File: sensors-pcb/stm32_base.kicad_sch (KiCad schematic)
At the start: 41 parts

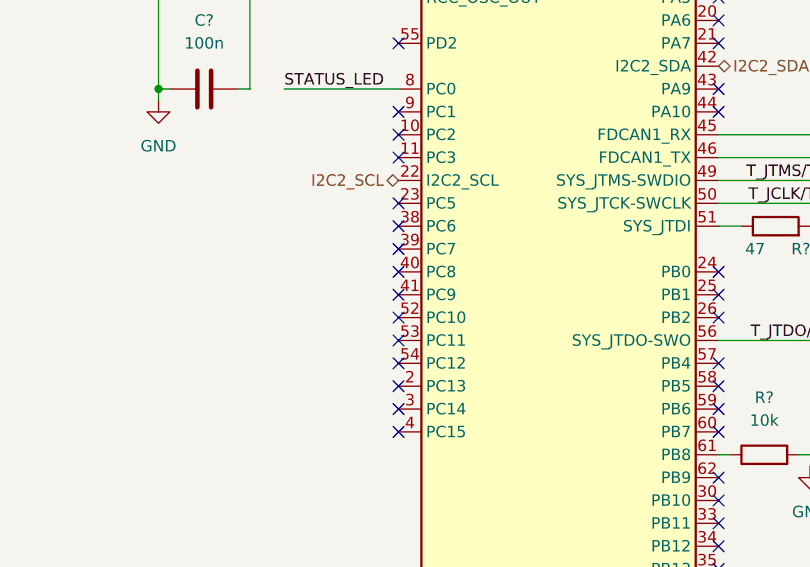
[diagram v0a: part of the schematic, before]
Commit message: sensors-pcb: finish GPS schematic
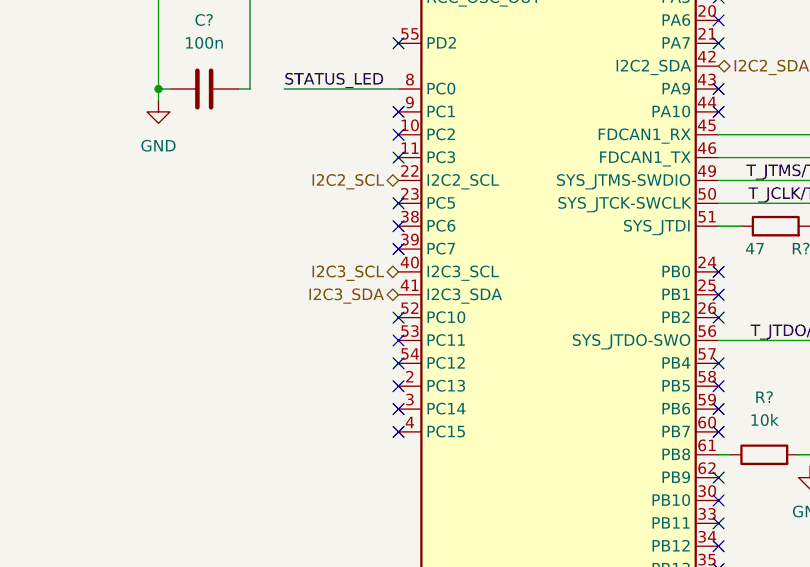
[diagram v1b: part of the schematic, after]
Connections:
- net I2C3_SCL: now reaches U?.40 (PC8)
- net I2C3_SDA: now reaches U?.41 (PC9)
- no-connect marks 40 -> 38
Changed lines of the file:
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@@
-	)
-	(no_connect
-		(at 63.5 138.43)
 	)
 	(no_connect
 		(at 63.5 113.03)
-	)
-	(no_connect
-		(at 63.5 140.97)
 	)
 	(no_connect
@@
 			)
 			(justify left)
+		)
+	)
+	(hierarchical_label "I2C3_SCL"
+		(shape bidirectional)
+		(at 63.5 138.43 180)
+		(effects
+			(font
+				(size 1.27 1.27)
+			)
+			(justify right)
+		)
+	)
+	(hierarchical_label "I2C3_SDA"
+		(shape bidirectional)
+		(at 63.5 140.97 180)
+		(effects
+			(font
+				(size 1.27 1.27)
+			)
+			(justify right)
 		)
 	)
@@
 		)
 		(pin "40"
+			(alternate "I2C3_SCL")
 		)
 		(pin "62"
@@
 		)
 		(pin "41"
+			(alternate "I2C3_SDA")
 		)
 		(pin "42"

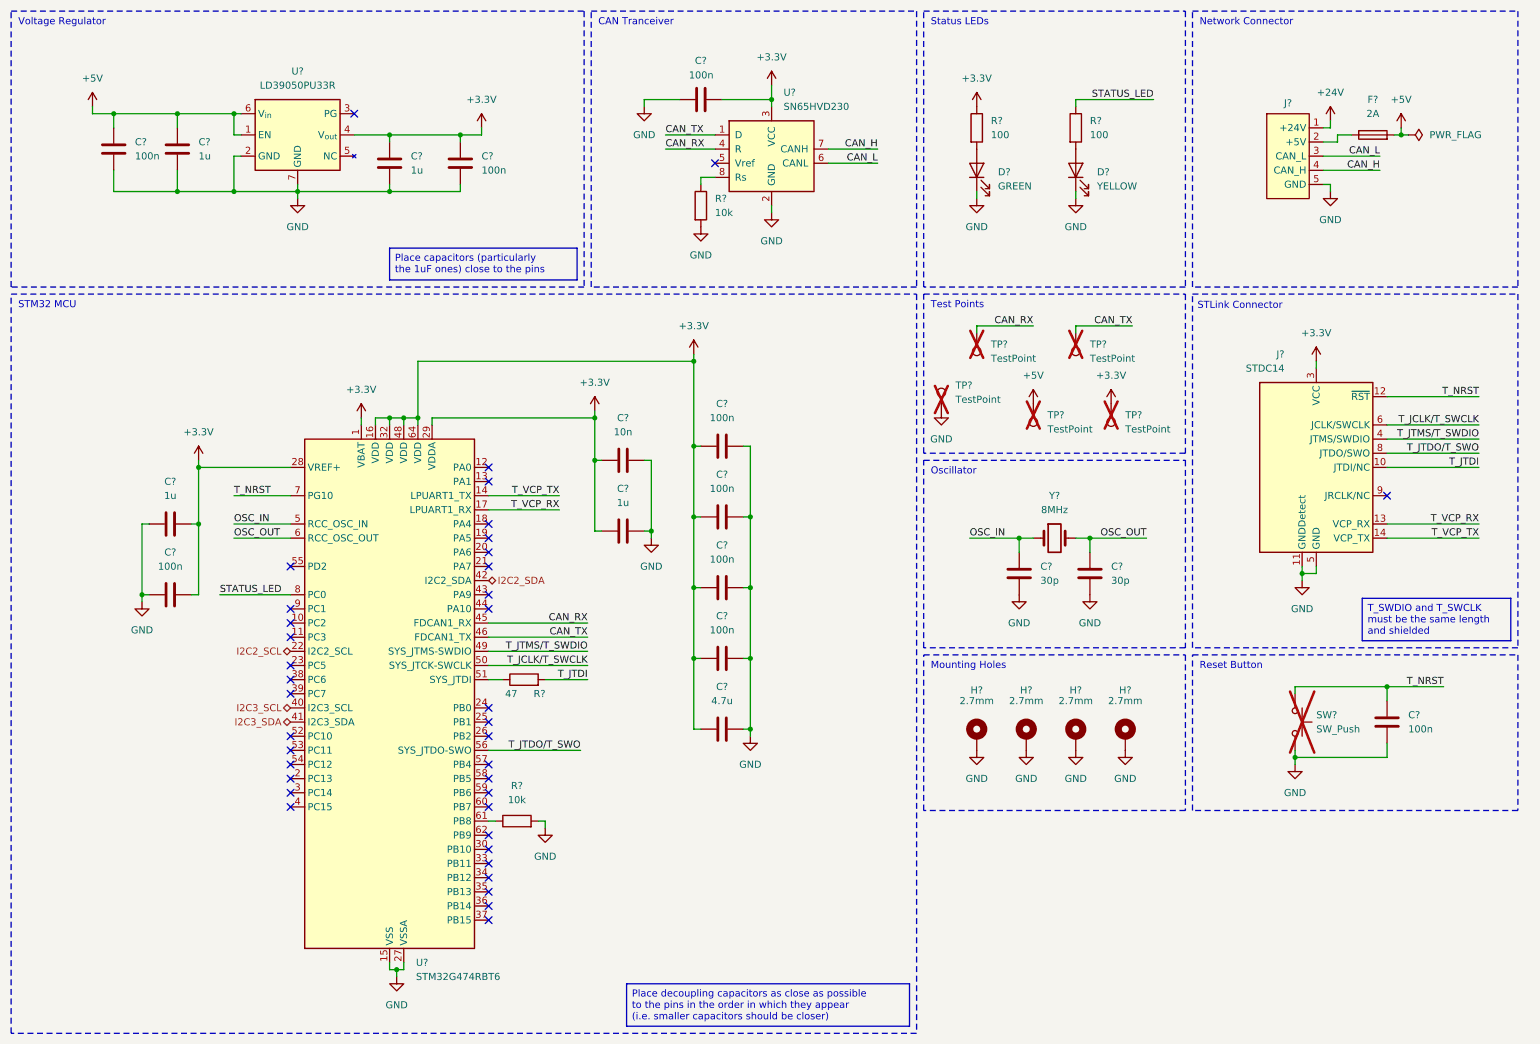
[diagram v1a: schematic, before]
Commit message: sensors-pcb: add footprints
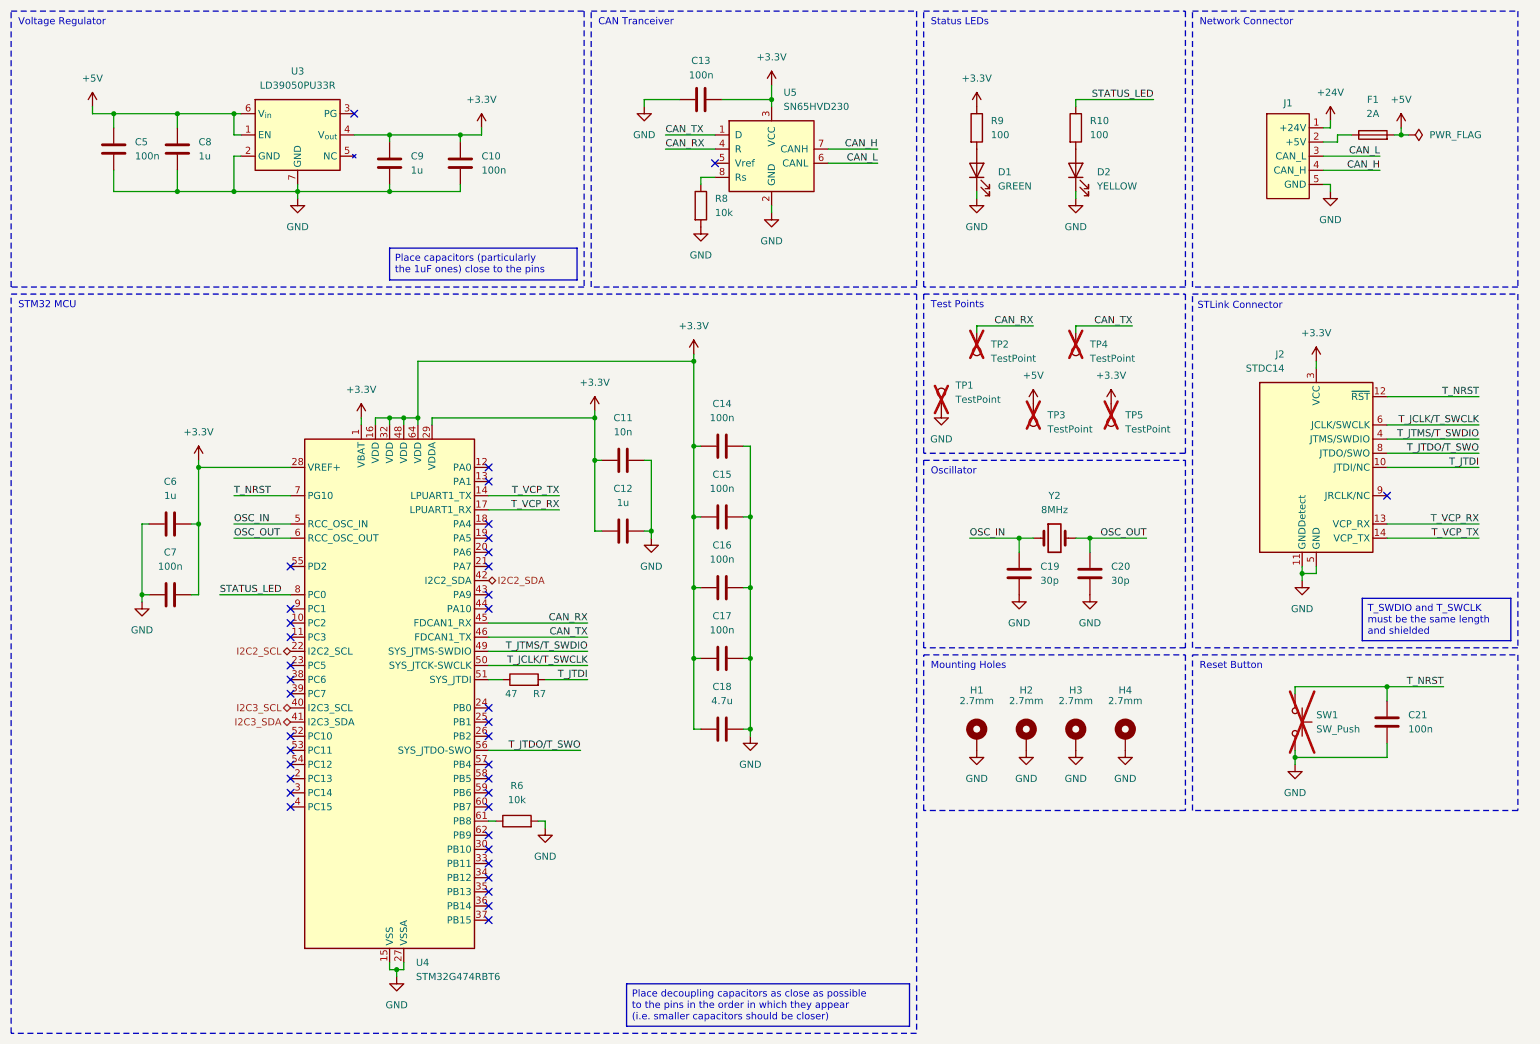
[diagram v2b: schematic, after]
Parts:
- gave numbers to parts that had none: 41

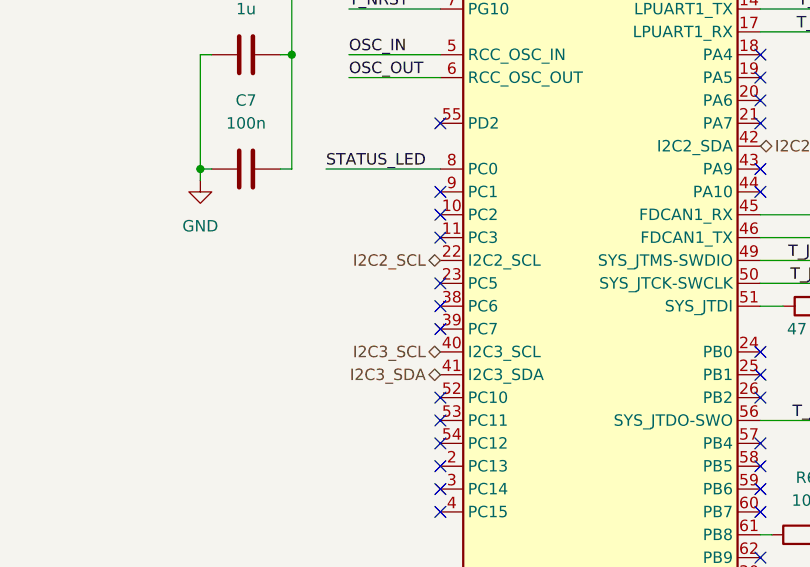
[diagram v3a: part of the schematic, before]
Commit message: sensors-pcb: replace IMU with MPU-6050
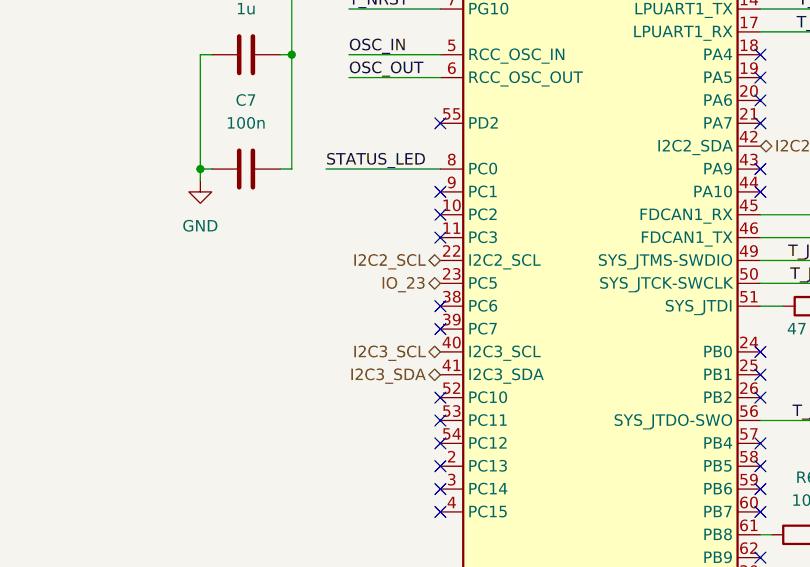
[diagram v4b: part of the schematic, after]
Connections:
- net IO_23: now reaches U4.23 (PC5)
- no-connect marks 38 -> 37
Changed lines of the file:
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@@
-	)
-	(no_connect
-		(at 63.5 130.81)
 	)
 	(no_connect
@@
 		)
 	)
+	(hierarchical_label "IO_23"
+		(shape bidirectional)
+		(at 63.5 130.81 180)
+		(effects
+			(font
+				(size 1.27 1.27)
+			)
+			(justify right)
+		)
+	)

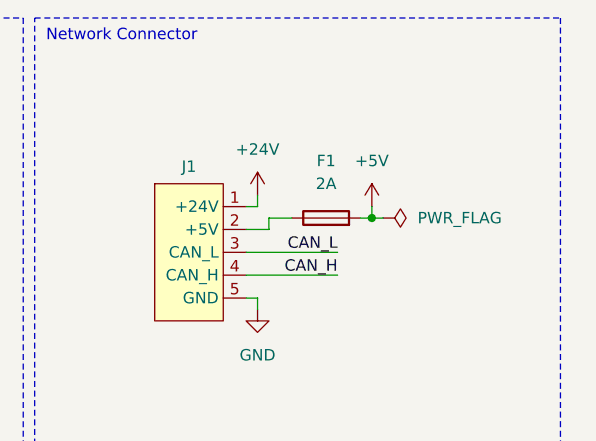
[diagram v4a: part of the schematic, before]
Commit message: sensors-pcb: add test point for fuse
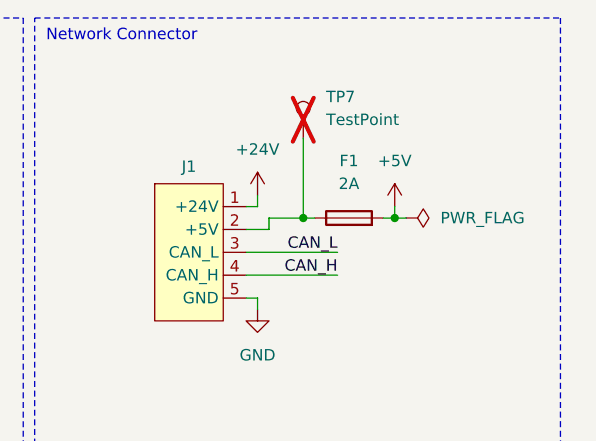
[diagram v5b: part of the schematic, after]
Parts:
- added TP4: TestPoint, TestPoint:TestPoint_Keystone_5005-5009_Compact, symbol Connector:TestPoint
- renumbered TP4 to TP7
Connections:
- net CAN_TX: now also TP4.1; no longer TP7.1
- net at F1.1, J1.2 (+5V): now also TP7.1
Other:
- moved on the sheet: F1, TP7
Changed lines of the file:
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@@
 	)
 	(junction
-		(at 262.89 35.56)
+		(at 265.43 35.56)
+		(diameter 0)
+		(color 0 0 0 0)
+	)
+	(junction
+		(at 255.27 35.56)
 		(diameter 0)
 		(color 0 0 0 0)
@@
 	(wire
 		(pts
-			(xy 251.46 35.56) (xy 254 35.56)
+			(xy 251.46 35.56) (xy 255.27 35.56)
 		)
 		(stroke
@@
 	(wire
 		(pts
-			(xy 262.89 34.29) (xy 262.89 35.56)
+			(xy 265.43 34.29) (xy 265.43 35.56)
 		)
 		(stroke
@@
 	(wire
 		(pts
-			(xy 261.62 35.56) (xy 262.89 35.56)
+			(xy 264.16 35.56) (xy 265.43 35.56)
 		)
 		(stroke
@@
 	(wire
 		(pts
-			(xy 262.89 35.56) (xy 264.16 35.56)
+			(xy 265.43 35.56) (xy 266.7 35.56)
 		)
 		(stroke
@@
 	(wire
 		(pts
+			(xy 256.54 35.56) (xy 255.27 35.56)
+		)
+		(stroke
+			(width 0)
+			(type default)
+		)
+	)
+	(wire
+		(pts
+			(xy 255.27 35.56) (xy 255.27 26.67)
+		)
+		(stroke
+			(width 0)
+			(type default)
+		)
+	)
+	(wire
+		(pts
 			(xy 146.05 104.14) (xy 146.05 116.84)
 		)
@@
 	(symbol
 		(lib_id "power:+5V")
-		(at 262.89 34.29 0)
+		(at 265.43 34.29 0)
 		(unit 1)
 		(exclude_from_sim no)
@@
 		(fields_autoplaced yes)
 		(property "Reference" "#PWR0132"
-			(at 262.89 38.1 0)
+			(at 265.43 38.1 0)
 			(effects
 				(font
@@
 		)
 		(property "Value" "+5V"
-			(at 262.89 29.21 0)
+			(at 265.43 29.21 0)
 			(effects
 				(font
@@
 		)
 		(property "Footprint" ""
-			(at 262.89 34.29 0)
+			(at 265.43 34.29 0)
 			(effects
 				(font
@@
 		)
 		(property "Datasheet" ""
-			(at 262.89 34.29 0)
+			(at 265.43 34.29 0)
 			(effects
 				(font
@@
 		)
 		(property "Description" "Power symbol creates a global label with name \"+5V\""
-			(at 262.89 34.29 0)
+			(at 265.43 34.29 0)
 			(effects
 				(font
@@
 	(symbol
 		(lib_id "Device:Fuse")
-		(at 257.81 35.56 90)
+		(at 260.35 35.56 90)
 		(unit 1)
 		(exclude_from_sim no)
@@
 		(fields_autoplaced yes)
 		(property "Reference" "F1"
-			(at 257.81 29.21 90)
+			(at 260.35 29.21 90)
 			(effects
 				(font
@@
 		)
 		(property "Value" "2A"
-			(at 257.81 31.75 90)
+			(at 260.35 31.75 90)
 			(effects
 				(font
@@
 		)
 		(property "Footprint" "Exocet:Fuse_Holder_Littelfuse_01530008"
-			(at 257.81 37.338 90)
+			(at 260.35 37.338 90)
 			(effects
 				(font
@@
 		)
 		(property "Datasheet" "~"
-			(at 257.81 35.56 0)
+			(at 260.35 35.56 0)
 			(effects
 				(font
@@
 		)
 		(property "Description" "Fuse"
-			(at 257.81 35.56 0)
+			(at 260.35 35.56 0)
 			(effects
 				(font
@@
 		)
 		(property "JLCPCB" "C206907"
-			(at 257.81 35.56 0)
+			(at 260.35 35.56 0)
 			(effects
 				(font
@@
 	(symbol
 		(lib_id "Connector:TestPoint")
+		(at 255.27 26.67 0)
+		(unit 1)
+		(exclude_from_sim no)
+		(in_bom yes)
+		(on_board yes)
+		(dnp yes)
+		(fields_autoplaced yes)
+		(property "Reference" "TP7"
+			(at 257.81 22.0979 0)
+			(effects
+				(font
+					(size 1.27 1.27)
+				)
+				(justify left)
+			)
+		)
+		(property "Value" "TestPoint"
+			(at 257.81 24.6379 0)
+			(effects
+				(font
+					(size 1.27 1.27)
+				)
+				(justify left)
+			)
+		)
+		(property "Footprint" "TestPoint:TestPoint_Keystone_5005-5009_Compact"
+			(at 260.35 26.67 0)
+			(effects
+				(font
+					(size 1.27 1.27)
+				)
+				(hide yes)
+			)
+		)
+		(property "Datasheet" "https://www.keyelco.com/userAssets/file/M65p56.pdf"
+			(at 260.35 26.67 0)
+			(effects
+				(font
+					(size 1.27 1.27)
+				)
+				(hide yes)
+			)
+		)
+		(property "Description" "test point"
+			(at 255.27 26.67 0)
+			(effects
+				(font
+					(size 1.27 1.27)
+				)
+				(hide yes)
+			)
+		)
+		(property "Net Label" "CAN_TX"
+			(at 255.27 26.67 0)
+			(effects
+				(font
+					(size 1.27 1.27)
+				)
+				(hide yes)
+			)
+		)
+		(pin "1"
+		)
+		(instances
+			(project "sensors-pcb"
+				(path "/4b4cf3aa-c94c-4150-b9c5-35049cd71136/7d59fd70-1fff-4c9c-ae77-583b08aef567"
+					(reference "TP7")
+					(unit 1)
+				)
+			)
+		)
+	)
+	(symbol
+		(lib_id "Connector:TestPoint")
 		(at 204.47 71.12 180)
 		(unit 1)
@@
 	(symbol
 		(lib_id "power:PWR_FLAG")
-		(at 264.16 35.56 270)
+		(at 266.7 35.56 270)
 		(unit 1)
 		(exclude_from_sim no)
@@
 		(fields_autoplaced yes)
 		(property "Reference" "#FLG0101"
-			(at 266.065 35.56 0)
+			(at 268.605 35.56 0)
 			(effects
 				(font
@@
 		)
 		(property "Value" "PWR_FLAG"
-			(at 267.97 35.5599 90)
+			(at 270.51 35.5599 90)
 			(effects
 				(font
@@
 		)
 		(property "Footprint" ""
-			(at 264.16 35.56 0)
+			(at 266.7 35.56 0)
 			(effects
 				(font
@@
 		)
 		(property "Datasheet" "~"
-			(at 264.16 35.56 0)
+			(at 266.7 35.56 0)
 			(effects
 				(font
@@
 		)
 		(property "Description" "Special symbol for telling ERC where power comes from"
-			(at 264.16 35.56 0)
+			(at 266.7 35.56 0)
 			(effects
 				(font

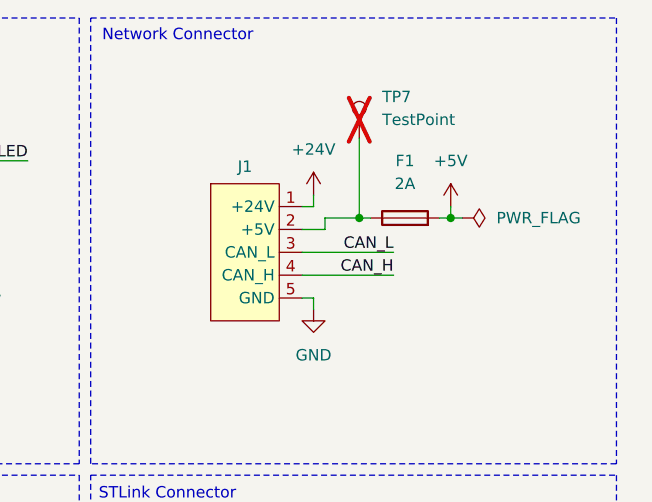
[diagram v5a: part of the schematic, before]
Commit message: sensors-pcb: change fuse to DNP
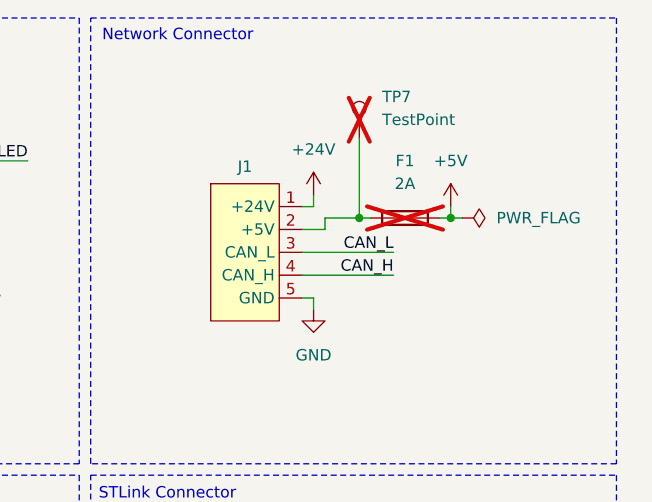
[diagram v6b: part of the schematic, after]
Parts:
- F1: now not fitted
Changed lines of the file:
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@@
 		(in_bom yes)
 		(on_board yes)
-		(dnp no)
+		(dnp yes)
 		(fields_autoplaced yes)
 		(property "Reference" "F1"

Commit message: sensors-pcb: ghost busted
fixed fuse test point label
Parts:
- TP7: Net Label CAN_TX -> +5v_in
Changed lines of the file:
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@@
 			)
 		)
-		(property "Net Label" "CAN_TX"
+		(property "Net Label" "+5v_in"
 			(at 255.27 26.67 0)
 			(effects

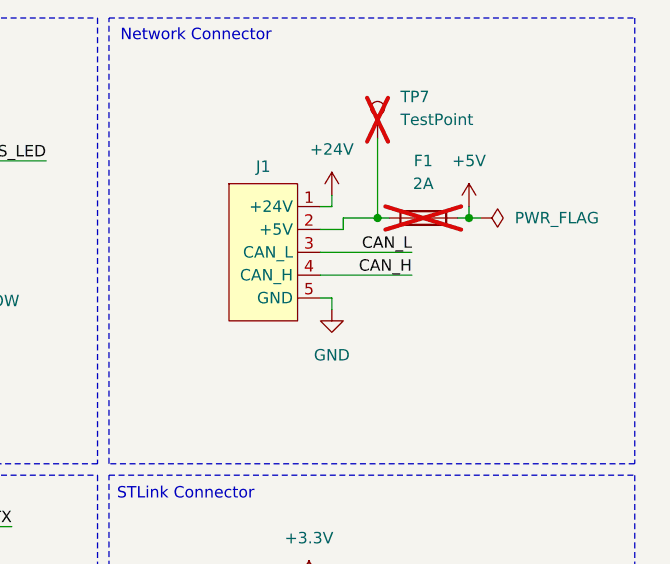
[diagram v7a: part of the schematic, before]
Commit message: sensors-pcb: add fuse holder 01110501Z
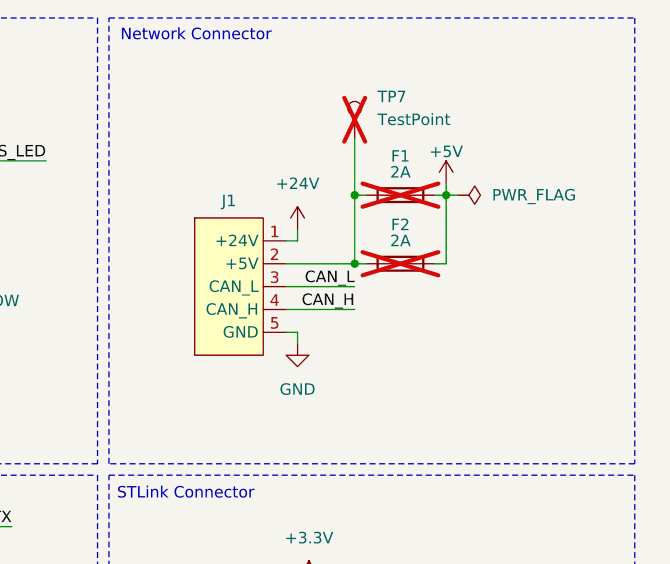
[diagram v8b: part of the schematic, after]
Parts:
- F2: renamed from F1; footprint Exocet:Fuse_Holder_Littelfuse_01530008 -> Fuse:Fuseholder_Clip-5x20mm_Littelfuse_111_Lateral_P18.80x5.00mm_D1.17mm_Horizontal; JLCPCB C206907 -> (none)
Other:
- moved on the sheet: F1, J1, TP7
